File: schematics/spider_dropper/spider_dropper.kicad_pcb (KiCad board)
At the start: 2 copper layers, 80 x 20 mm, 11 parts, among them J1 12V DC, J2 Sensor, J3 Motor, Q1 2N3904, Q2 TIP120, SW1 ZX40E10C01

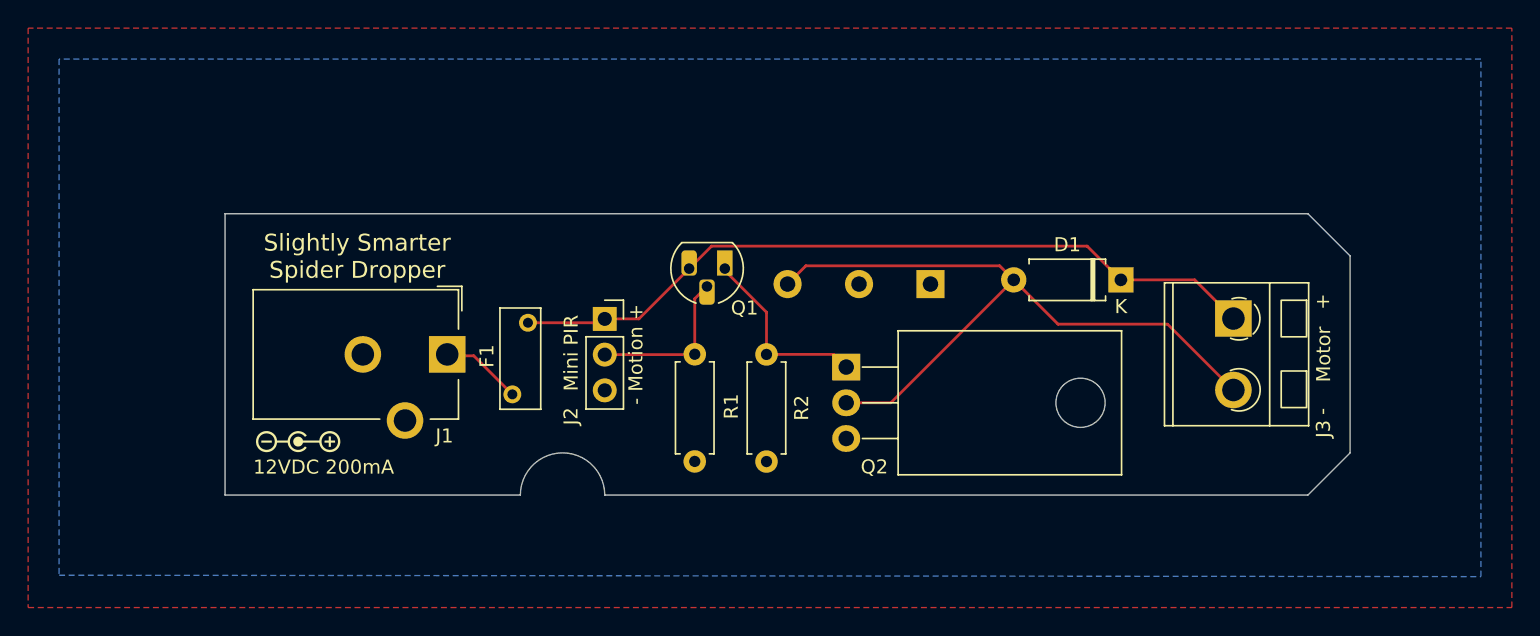
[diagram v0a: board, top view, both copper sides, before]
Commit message: Re-oriented and re-position the PCB and cradle.
Also gave each printed part a unique color in preview.

Rev A boards ordered from this commit.
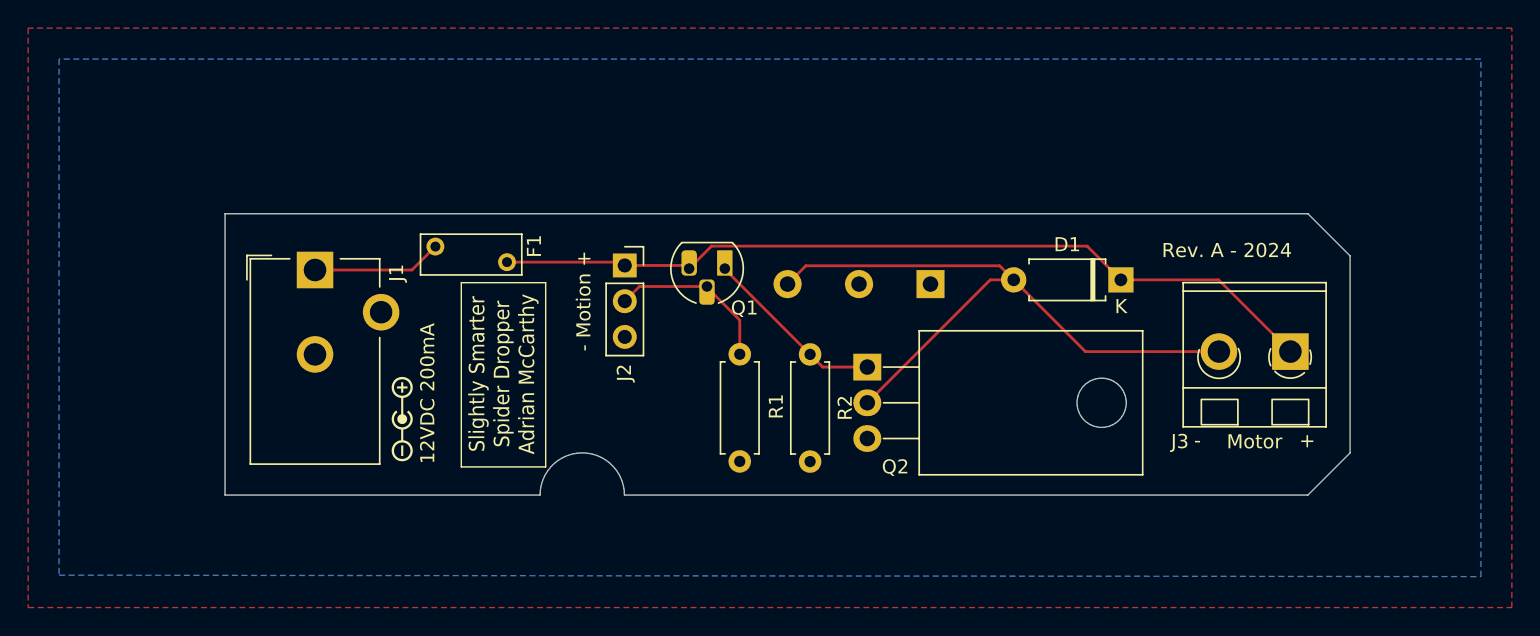
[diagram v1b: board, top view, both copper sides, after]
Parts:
- moved F1 11.8 mm to (124.9, 100.6), turned to 0 degrees
- moved J1 11.2 mm to (116.3, 102.3), turned to 0 degrees
- moved G1 7.57 mm to (122.5, 112.9), turned to 90 degrees
- moved J3 4.68 mm to (185.7, 108.1), turned to 180 degrees
- moved J2 4.06 mm to (138.3, 102.0)
- moved R1 3.20 mm to (146.5, 108.3)
- moved R2 3.10 mm to (151.5, 108.3)
- moved Q2 1.50 mm to (155.6, 109.2)
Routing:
- net Net-(D1-K): track 54.6 -> 59.7 mm
- net Net-(D1-A): track 51.4 -> 47.8 mm
- net +12V: track 5.81 -> 9.25 mm
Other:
- outline, holes or cut-outs redrawn
- board text added: "Rev. A - 2024"
- board text added: "Slightly Smarter Spider Dropper Adrian McCarthy"
- board text removed: "Mini PIR"
- board text removed: "Slightly Smarter Spider Dropper"

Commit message: Updated PCB layout (now Rev. B) for more clearance around connectors.
The motion sensor header was within the margin, but the motion sensor
itself would run into the edge of the deeper cradle.  I centered it
on the short axis and aligned it with the index post on the long axis.
This should enable the cradle to have some supports for the sensor
module or a cable that connects to it.
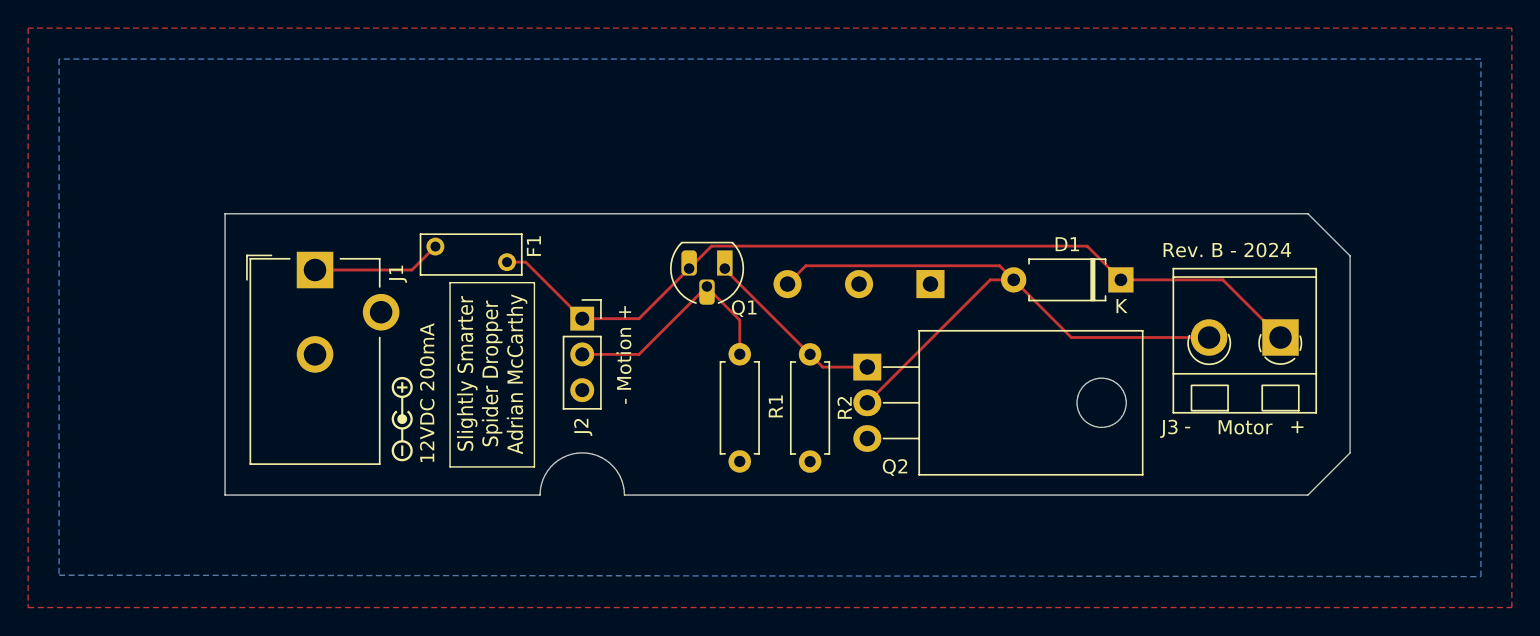
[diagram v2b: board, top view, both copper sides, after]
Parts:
- moved J2 4.85 mm to (135.3, 105.8)
- moved J3 1.22 mm to (184.9, 107.1)
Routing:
- net Net-(J2-Pin_2): track 12.1 -> 16.7 mm
- net Net-(D1-K): track 59.7 -> 61.9 mm
- net Net-(D1-A): track 47.8 -> 46.7 mm
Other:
- board text added: "Rev. B - 2024"
- board text removed: "Rev. A - 2024"
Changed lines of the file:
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@@
 	(title_block
 		(title "Slightly Smarter Simple Spider Dropper")
-		(date "2024-11-29")
-		(rev "A")
+		(date "2024-12-22")
+		(rev "B")
 		(company "Adrian McCarthy")
+		(comment 1 "Improved clearance around J2 and J3")
 	)
 	(layers
@@
 	(footprint "Connector_PinSocket_2.54mm:PinSocket_1x03_P2.54mm_Vertical"
 		(layer "F.Cu")
-		(at 138.325 101.975)
+		(at 135.3 105.76)
 		(descr "Through hole straight socket strip, 1x03, 2.54mm pitch, single row (from Kicad 4.0.7), script generated")
 		(tags "Through hole socket strip THT 1x03 2.54mm single row")
@@
 	(footprint "aid_Connector:CUI_TB007-508_01x02_THT_Screw_Terminal_Block"
 		(layer "F.Cu")
-		(at 185.65 108.1 180)
+		(at 184.95 107.1 180)
 		(property "Reference" "J3"
 			(at 7.85 -6.4 0)
@@
 	)
 	(gr_rect
-		(start 126.7 103.2)
-		(end 132.7 116.3)
+		(start 125.9 103.2)
+		(end 131.9 116.3)
 		(stroke
 			(width 0.1)
@@
 	)
 	(gr_text "- Motion +"
-		(at 136 104.5 90)
+		(at 138.9 108.3 90)
 		(layer "F.SilkS")
 		(effects
@@
 		)
 	)
-	(gr_text "Rev. A - 2024"
+	(gr_text "Rev. B - 2024"
 		(at 176.5 101.5 0)
 		(layer "F.SilkS")
@@
 	)
 	(gr_text "-"
-		(at 178.8 115 0)
+		(at 178.1 114 0)
 		(layer "F.SilkS")
 		(effects
@@
 	)
 	(gr_text "Motor"
-		(at 183.1 115.1 0)
+		(at 182.4 114.1 0)
 		(layer "F.SilkS")
 		(effects
@@
 	)
 	(gr_text "Slightly Smarter\nSpider Dropper\nAdrian McCarthy"
-		(at 129.6 109.7 90)
+		(at 128.8 109.7 90)
 		(layer "F.SilkS")
 		(effects
@@
 	)
 	(gr_text "+"
-		(at 186.3 113.9 -90)
+		(at 185.6 112.9 -90)
 		(layer "F.SilkS")
 		(effects
@@
 	)
 	(segment
-		(start 165.98 103)
-		(end 164.31 103)
+		(start 179.87 107.1)
+		(end 170.08 107.1)
 		(width 0.2)
 		(layer "F.Cu")
@@
 	)
 	(segment
-		(start 164.98 102)
-		(end 151.2 102)
+		(start 170.08 107.1)
+		(end 165.98 103)
 		(width 0.2)
 		(layer "F.Cu")
@@
 	)
 	(segment
-		(start 171.08 108.1)
-		(end 180.57 108.1)
+		(start 165.98 103)
+		(end 164.31 103)
 		(width 0.2)
 		(layer "F.Cu")
@@
 	)
 	(segment
-		(start 165.98 103)
-		(end 171.08 108.1)
+		(start 164.98 102)
+		(end 151.2 102)
 		(width 0.2)
 		(layer "F.Cu")
@@
 	)
 	(segment
-		(start 139.37 103.47)
-		(end 144.17 103.47)
+		(start 146.5 105.86)
+		(end 146.5 108.29)
 		(width 0.2)
 		(layer "F.Cu")
@@
 	)
 	(segment
-		(start 146.5 105.86)
-		(end 146.5 108.29)
+		(start 144.17 103.47)
+		(end 139.34 108.3)
 		(width 0.2)
 		(layer "F.Cu")
@@
 	)
 	(segment
-		(start 138.325 104.515)
-		(end 139.37 103.47)
+		(start 139.34 108.3)
+		(end 135.3 108.3)
 		(width 0.2)
 		(layer "F.Cu")
@@
 	)
 	(segment
-		(start 129.95 101.74)
-		(end 138.09 101.74)
+		(start 180.85 103)
+		(end 184.95 107.1)
 		(width 0.2)
 		(layer "F.Cu")
@@
 	)
 	(segment
-		(start 138.325 101.975)
-		(end 142.675 101.975)
+		(start 135.3 105.76)
+		(end 139.34 105.76)
 		(width 0.2)
 		(layer "F.Cu")
@@
 	)
 	(segment
-		(start 142.9 102.2)
-		(end 144.5 100.6)
+		(start 173.6 103)
+		(end 180.85 103)
 		(width 0.2)
 		(layer "F.Cu")
@@
 	)
 	(segment
-		(start 173.47 102.7)
-		(end 173.41 102.7)
+		(start 129.95 101.74)
+		(end 131.28 101.74)
 		(width 0.2)
 		(layer "F.Cu")
@@
 	)
 	(segment
-		(start 142.675 101.975)
+		(start 142.9 102.2)
+		(end 144.5 100.6)
+		(width 0.2)
+		(layer "F.Cu")
+		(net 8)
+	)
+	(segment
+		(start 139.34 105.76)
 		(end 142.9 102.2)
 		(width 0.2)
@@
 	)
 	(segment
-		(start 144.5 100.6)
-		(end 171.2 100.6)
+		(start 173.47 102.7)
+		(end 173.41 102.7)
 		(width 0.2)
 		(layer "F.Cu")
@@
 	)
 	(segment
-		(start 180.55 103)
-		(end 185.65 108.1)
+		(start 142.675 101.975)
+		(end 142.9 102.2)
 		(width 0.2)
 		(layer "F.Cu")
@@
 	)
 	(segment
-		(start 138.09 101.74)
-		(end 138.325 101.975)
+		(start 144.5 100.6)
+		(end 171.2 100.6)
 		(width 0.2)
 		(layer "F.Cu")
@@
 	)
 	(segment
-		(start 173.6 103)
-		(end 180.55 103)
+		(start 131.28 101.74)
+		(end 135.3 105.76)
 		(width 0.2)
 		(layer "F.Cu")

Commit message: More PCB layout tweaks to ease assembly.
Power connector is closer to cradle wall so that there's enough room
for a fat plug.

Fuse and TIP120 are in a little more from the edges.

Resistors and BJT are shifted to space out the pads for easier
soldering.
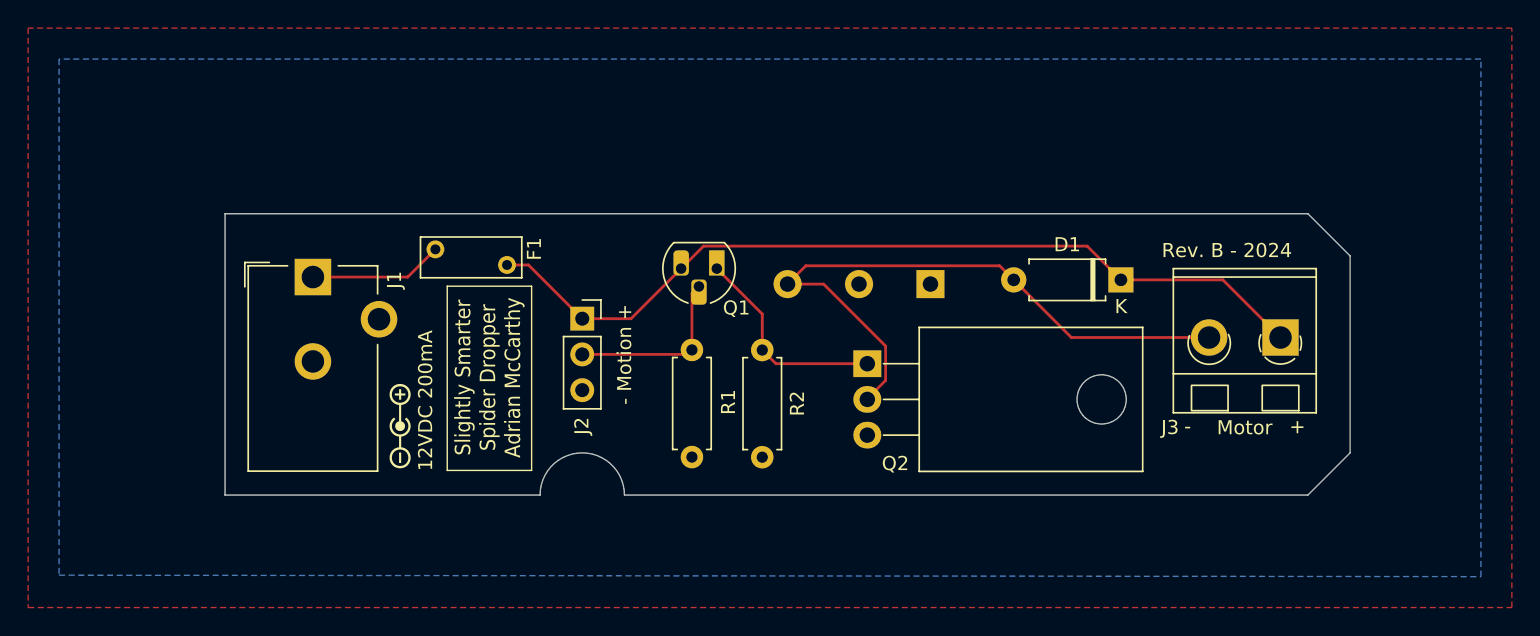
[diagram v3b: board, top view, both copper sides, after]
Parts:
- moved R1 3.41 mm to (143.1, 108.0)
- moved R2 3.41 mm to (148.1, 108.0)
- moved Q1 0.57 mm to (144.9, 102.2)
- moved G1 0.52 mm to (122.3, 113.4)
- moved J1 0.52 mm to (116.2, 102.8)
- moved Q2 0.24 mm to (155.6, 109.0)
- moved F1 0.20 mm to (124.9, 100.8)
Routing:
- net Net-(J2-Pin_2): track 16.7 -> 12.6 mm
- net Net-(Q1-E): track 13.3 -> 15.0 mm
- net Net-(D1-A): track 46.7 -> 45.7 mm
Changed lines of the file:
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@@
 	(footprint "Resistor_THT:R_Axial_DIN0207_L6.3mm_D2.5mm_P7.62mm_Horizontal"
 		(layer "F.Cu")
-		(at 151.5 108.3 -90)
+		(at 148.1 107.99 -90)
 		(descr "Resistor, Axial_DIN0207 series, Axial, Horizontal, pin pitch=7.62mm, 0.25W = 1/4W, length*diameter=6.3*2.5mm^2, http://cdn-reichelt.de/documents/datenblatt/B400/1_4W%23YAG.pdf")
 		(tags "Resistor Axial_DIN0207 series Axial Horizontal pin pitch 7.62mm 0.25W = 1/4W length 6.3mm diameter 2.5mm")
@@
 	(footprint "Resistor_THT:R_Axial_DIN0207_L6.3mm_D2.5mm_P7.62mm_Horizontal"
 		(layer "F.Cu")
-		(at 146.5 108.29 -90)
+		(at 143.1 107.98 -90)
 		(descr "Resistor, Axial_DIN0207 series, Axial, Horizontal, pin pitch=7.62mm, 0.25W = 1/4W, length*diameter=6.3*2.5mm^2, http://cdn-reichelt.de/documents/datenblatt/B400/1_4W%23YAG.pdf")
 		(tags "Resistor Axial_DIN0207 series Axial Horizontal pin pitch 7.62mm 0.25W = 1/4W length 6.3mm diameter 2.5mm")
@@
 	(footprint "Connector_BarrelJack:BarrelJack_CUI_PJ-102AH_Horizontal"
 		(layer "F.Cu")
-		(at 116.3 102.3)
+		(at 116.15 102.8)
 		(descr "Thin-pin DC Barrel Jack, https://cdn-shop.adafruit.com/datasheets/21mmdcjackDatasheet.pdf")
 		(tags "Power Jack")
@@
 	(footprint "Package_TO_SOT_THT:TO-220-3_Horizontal_TabDown"
 		(layer "F.Cu")
-		(at 155.57 109.2 -90)
+		(at 155.57 108.96 -90)
 		(descr "TO-220-3, Horizontal, RM 2.54mm, see https://www.vishay.com/docs/66542/to-220-1.pdf")
 		(tags "TO-220-3 Horizontal RM 2.54mm")
@@
 	(footprint "aid_Switch:Fuse_BelFuse_0ZRC_L7.4mm_W3.1mm"
 		(layer "F.Cu")
-		(at 124.86 100.63)
+		(at 124.86 100.83)
 		(descr "Fuse 0ZRC, BelFuse, Radial Leaded PTC, https://www.belfuse.com/resources/datasheets/circuitprotection/ds-cp-0zrc-series.pdf")
 		(tags "0ZRC BelFuse radial PTC")
@@
 	(footprint "aid_Symbols_Icons:PolarityCenterPositive_6x1.5mm_Silkscreen"
 		(layer "F.Cu")
-		(at 122.5 112.9 90)
+		(at 122.35 113.4 90)
 		(property "Reference" "G1"
 			(at 0 0 90)
@@
 	(footprint "Package_TO_SOT_THT:TO-92_HandSolder"
 		(layer "F.Cu")
-		(at 145.44 102.2 180)
+		(at 144.87 102.2 180)
 		(descr "TO-92 leads molded, narrow, drill 0.75mm, handsoldering variant with enlarged pads (see NXP sot054_po.pdf)")
 		(tags "to-92 sc-43 sc-43a sot54 PA33 transistor")
@@
 	)
 	(gr_rect
-		(start 125.9 103.2)
-		(end 131.9 116.3)
+		(start 125.7 103.45)
+		(end 131.7 116.55)
 		(stroke
 			(width 0.1)
@@
 	)
 	(gr_text "12VDC 200mA"
-		(at 124.9 116.1 90)
+		(at 124.75 116.6 90)
 		(layer "F.SilkS")
 		(effects
@@
 	)
 	(gr_text "Slightly Smarter\nSpider Dropper\nAdrian McCarthy"
-		(at 128.8 109.7 90)
+		(at 128.6 109.95 90)
 		(layer "F.SilkS")
 		(effects
@@
 	)
 	(segment
-		(start 116.3 102.3)
-		(end 123.19 102.3)
+		(start 122.89 102.8)
+		(end 124.86 100.83)
 		(width 0.2)
 		(layer "F.Cu")
@@
 	)
 	(segment
-		(start 123.19 102.3)
-		(end 124.86 100.63)
+		(start 116.15 102.8)
+		(end 122.89 102.8)
 		(width 0.2)
 		(layer "F.Cu")
@@
 	)
 	(segment
+		(start 155.57 111.4525)
+		(end 156.87 110.1525)
+		(width 0.2)
+		(layer "F.Cu")
+		(net 2)
+	)
+	(segment
 		(start 165.98 103)
 		(end 164.98 102)
@@
 	)
 	(segment
-		(start 165.98 103)
-		(end 164.31 103)
+		(start 164.98 102)
+		(end 151.2 102)
 		(width 0.2)
 		(layer "F.Cu")
@@
 	)
 	(segment
-		(start 164.98 102)
-		(end 151.2 102)
+		(start 156.87 107.7075)
+		(end 152.4625 103.3)
 		(width 0.2)
 		(layer "F.Cu")
@@
 	)
 	(segment
-		(start 164.31 103)
-		(end 155.57 111.74)
+		(start 152.4625 103.3)
+		(end 149.9 103.3)
 		(width 0.2)
 		(layer "F.Cu")
@@
 	)
 	(segment
-		(start 144.17 103.47)
-		(end 144.2 103.5)
+		(start 155.57 111.5)
+		(end 155.57 111.4525)
 		(width 0.2)
 		(layer "F.Cu")
-		(net 5)
+		(net 2)
 	)
 	(segment
-		(start 144.17 103.53)
-		(end 146.5 105.86)
+		(start 156.87 110.1525)
+		(end 156.87 107.7075)
 		(width 0.2)
 		(layer "F.Cu")
-		(net 5)
+		(net 2)
 	)
 	(segment
-		(start 144.17 103.47)
-		(end 144.17 103.53)
+		(start 143.6 103.47)
+		(end 143.1 103.97)
 		(width 0.2)
 		(layer "F.Cu")
@@
 	)
 	(segment
-		(start 146.5 105.86)
-		(end 146.5 108.29)
+		(start 142.78 108.3)
+		(end 143.1 107.98)
 		(width 0.2)
 		(layer "F.Cu")
@@
 	)
 	(segment
-		(start 144.17 103.47)
-		(end 139.34 108.3)
+		(start 143.1 103.97)
+		(end 143.1 107.98)
 		(width 0.2)
 		(layer "F.Cu")
@@
 	)
 	(segment
-		(start 139.34 108.3)
-		(end 135.3 108.3)
+		(start 135.3 108.3)
+		(end 142.78 108.3)
 		(width 0.2)
 		(layer "F.Cu")
@@
 	)
 	(segment
-		(start 145.5 102.2)
-		(end 145.44 102.2)
+		(start 148.1 107.99)
+		(end 148.1 105.43)
 		(width 0.2)
 		(layer "F.Cu")
@@
 	)
 	(segment
-		(start 152.4 109.2)
-		(end 151.5 108.3)
+		(start 148.1 105.43)
+		(end 144.87 102.2)
 		(width 0.2)
 		(layer "F.Cu")
@@
 	)
 	(segment
-		(start 151.5 108.3)
-		(end 145.44 102.24)
+		(start 149.07 108.96)
+		(end 148.1 107.99)
 		(width 0.2)
 		(layer "F.Cu")
@@
 	)
 	(segment
-		(start 145.44 102.24)
-		(end 145.44 102.2)
+		(start 155.57 108.96)
+		(end 149.07 108.96)
 		(width 0.2)
 		(layer "F.Cu")
@@
 	)
 	(segment
-		(start 145.44 102.2)
-		(end 145.44 102.34)
+		(start 180.85 103)
+		(end 184.95 107.1)
 		(width 0.2)
 		(layer "F.Cu")
-		(net 6)
+		(net 8)
 	)
 	(segment
-		(start 155.57 109.2)
-		(end 152.4 109.2)
+		(start 135.3 105.76)
+		(end 138.77 105.76)
 		(width 0.2)
 		(layer "F.Cu")
-		(net 6)
+		(net 8)
 	)
 	(segment
@@
 	)
 	(segment
-		(start 180.85 103)
-		(end 184.95 107.1)
-		(width 0.2)
-		(layer "F.Cu")
-		(net 8)
-	)
-	(segment
-		(start 135.3 105.76)
-		(end 139.34 105.76)
+		(start 143.93 100.6)
+		(end 171.2 100.6)
 		(width 0.2)
 		(layer "F.Cu")
@@
 	)
 	(segment
-		(start 129.95 101.74)
-		(end 131.28 101.74)
-		(width 0.2)
-		(layer "F.Cu")
-		(net 8)
-	)
-	(segment
-		(start 142.9 102.2)
-		(end 144.5 100.6)
-		(width 0.2)
-		(layer "F.Cu")
-		(net 8)
-	)
-	(segment
-		(start 139.34 105.76)
-		(end 142.9 102.2)
+		(start 173.47 102.7)
+		(end 173.41 102.7)
 		(width 0.2)
 		(layer "F.Cu")
@@
 	)
 	(segment
-		(start 173.47 102.7)
-		(end 173.41 102.7)
+		(start 138.77 105.76)
+		(end 142.33 102.2)
 		(width 0.2)
 		(layer "F.Cu")
@@
 	)
 	(segment
-		(start 142.675 101.975)
-		(end 142.9 102.2)
+		(start 131.48 101.94)
+		(end 135.3 105.76)
 		(width 0.2)
 		(layer "F.Cu")
@@
 	)
 	(segment
-		(start 144.5 100.6)
-		(end 171.2 100.6)
+		(start 142.33 102.2)
+		(end 143.93 100.6)
 		(width 0.2)
 		(layer "F.Cu")
@@
 	)
 	(segment
-		(start 131.28 101.74)
-		(end 135.3 105.76)
+		(start 129.95 101.94)
+		(end 131.48 101.94)
 		(width 0.2)
 		(layer "F.Cu")
